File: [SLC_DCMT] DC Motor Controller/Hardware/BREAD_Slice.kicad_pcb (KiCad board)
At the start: 2 copper layers, 70 x 100 mm, 46 parts, among them J1 Conn_01x10_Female, J10 Term_PressFit_Phoenix_Contact, J11 Term_PressFit_Phoenix_Contact, J12 cap, J13 Term_PressFit_Phoenix_Contact, J14 cap, J15 Term_PressFit_Phoenix_Contact, J16 Term_PressFit_Phoenix_Contact, J17 Term_PressFit_Phoenix_Contact, J18 I2C_01x04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

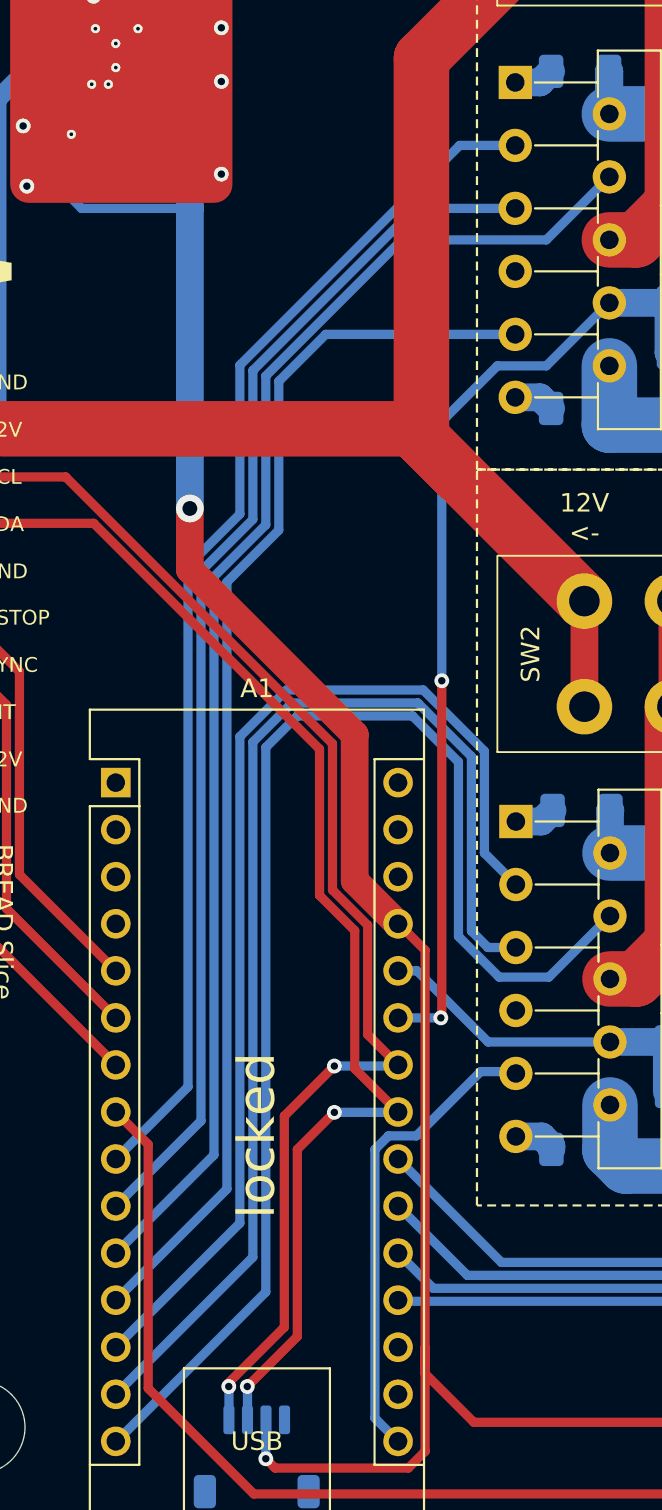
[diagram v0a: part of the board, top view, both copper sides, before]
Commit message: Updated DCMT pin connections
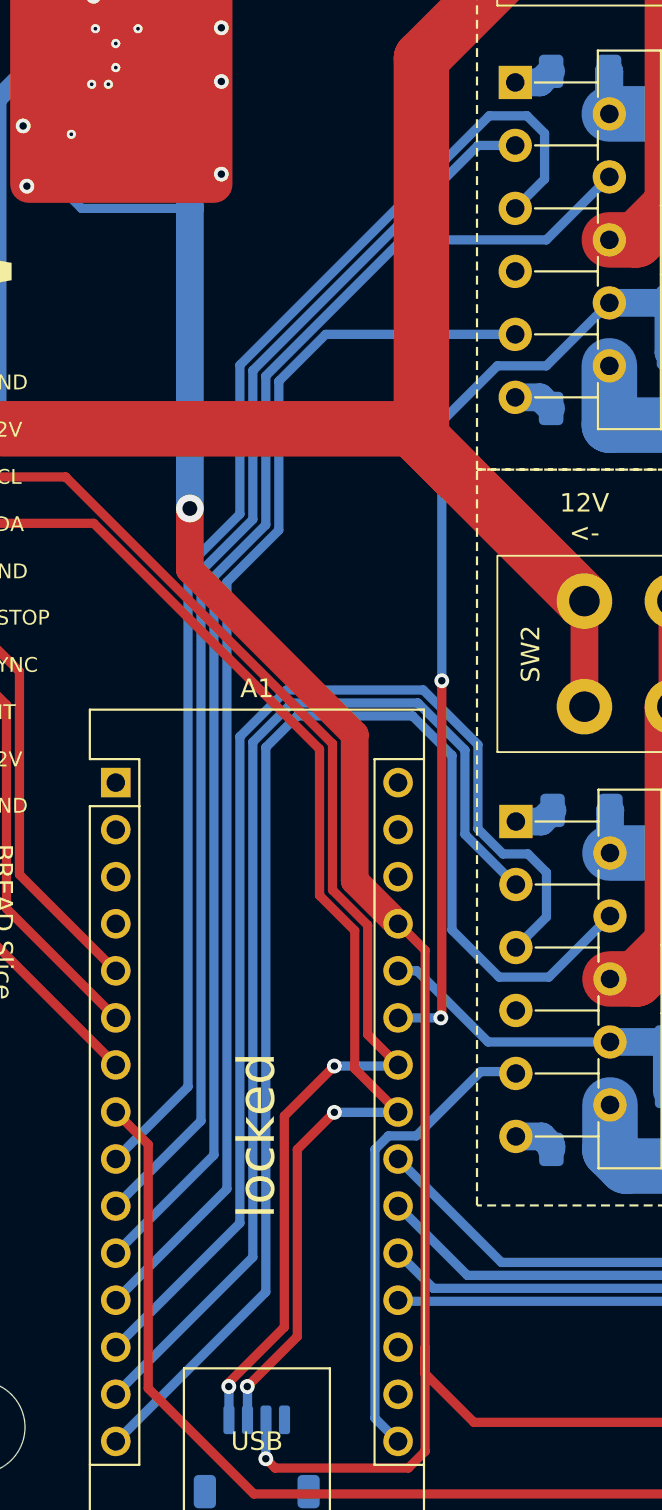
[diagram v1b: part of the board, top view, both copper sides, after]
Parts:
- J12, J14, J6: value cap -> Term_PressFit_Phoenix_Contact
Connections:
- A1 pad 10: /MC1 -> /DIR1
- A1 pad 13: /DIR2 -> /MC2
- A1 pad 14: /MC2 -> /DIR2
- A1 pad 9: /DIR1 -> /MC1
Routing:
- net /MC1: track 66.0 -> 72.8 mm
- net /DIR1: track 65.4 -> 67.4 mm
- net /DIR2: track 59.3 -> 60.1 mm
